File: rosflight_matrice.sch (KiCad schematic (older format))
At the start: 18 parts, among them J1 Left, J10 I2C, J11 I2C, J2 Right, J3 Power, J4 Servo 1-3, J5 Servo 4-6, J6 Main, J7 Flexi-IO, J8 Flexi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

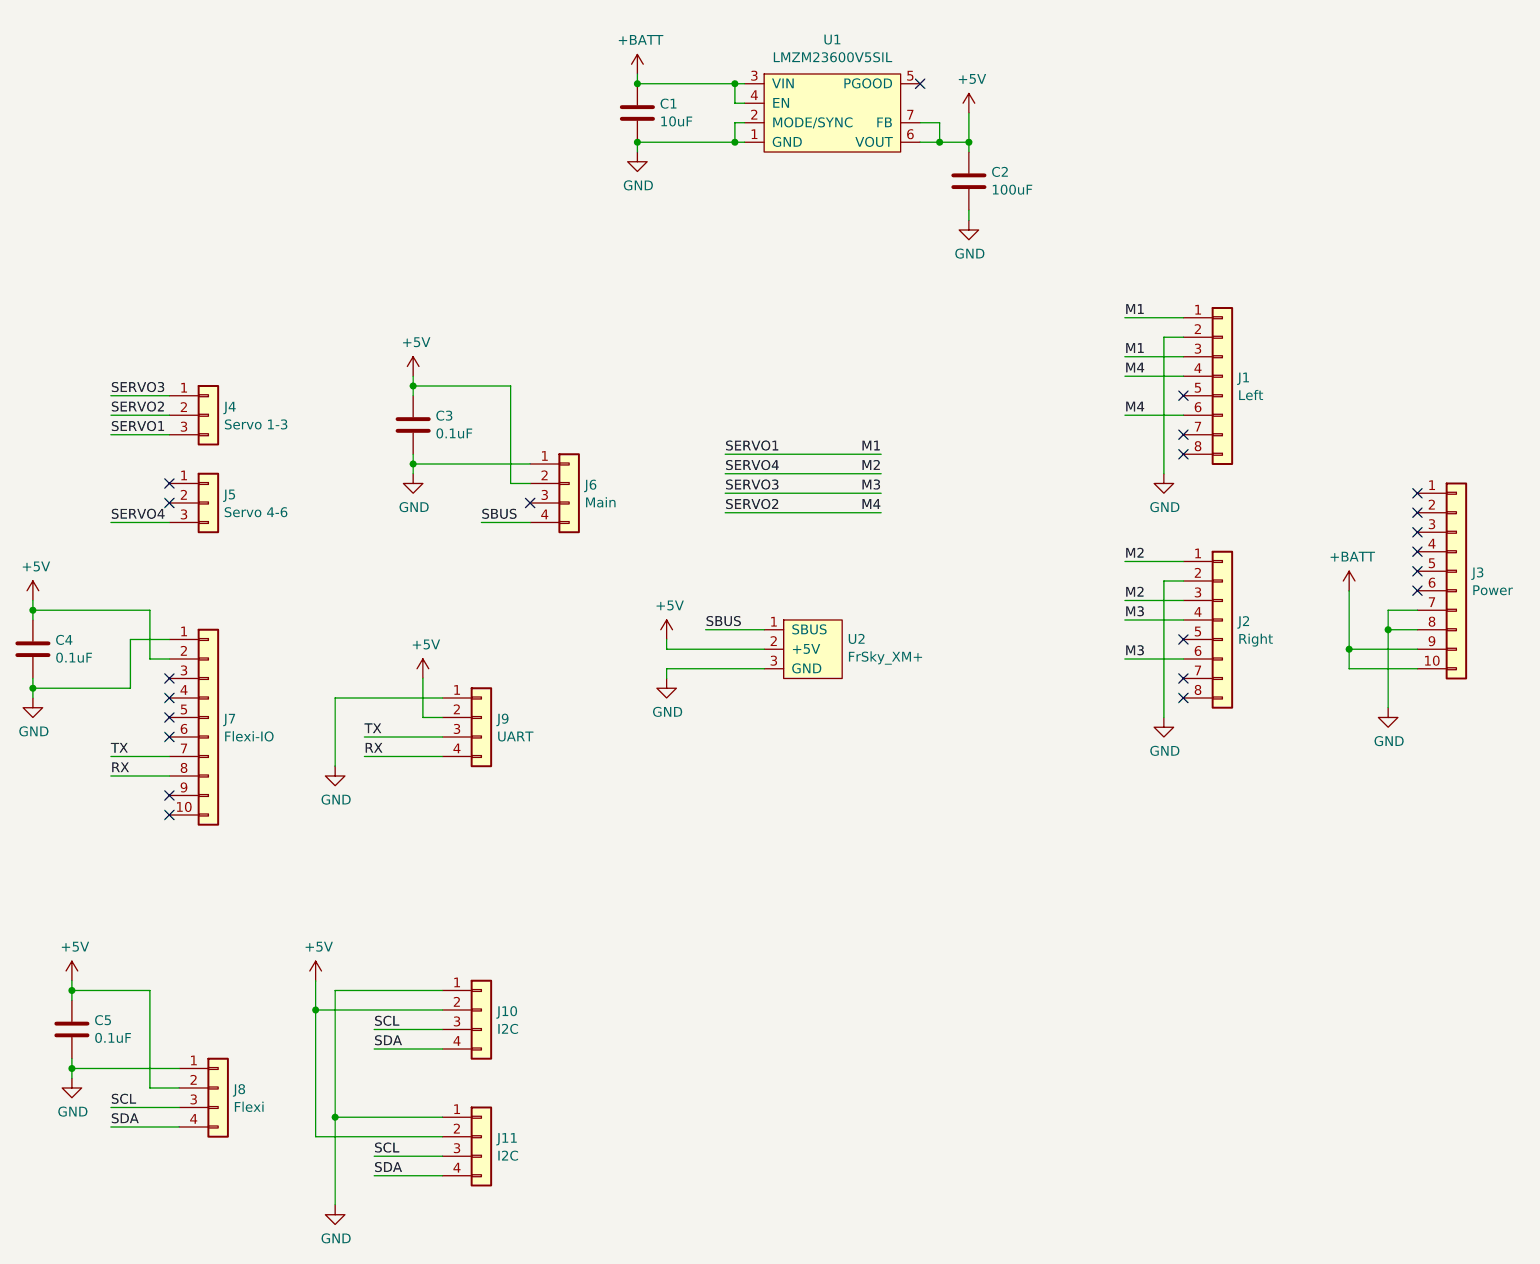
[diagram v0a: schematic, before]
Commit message: New switching voltage regulator and updated layout
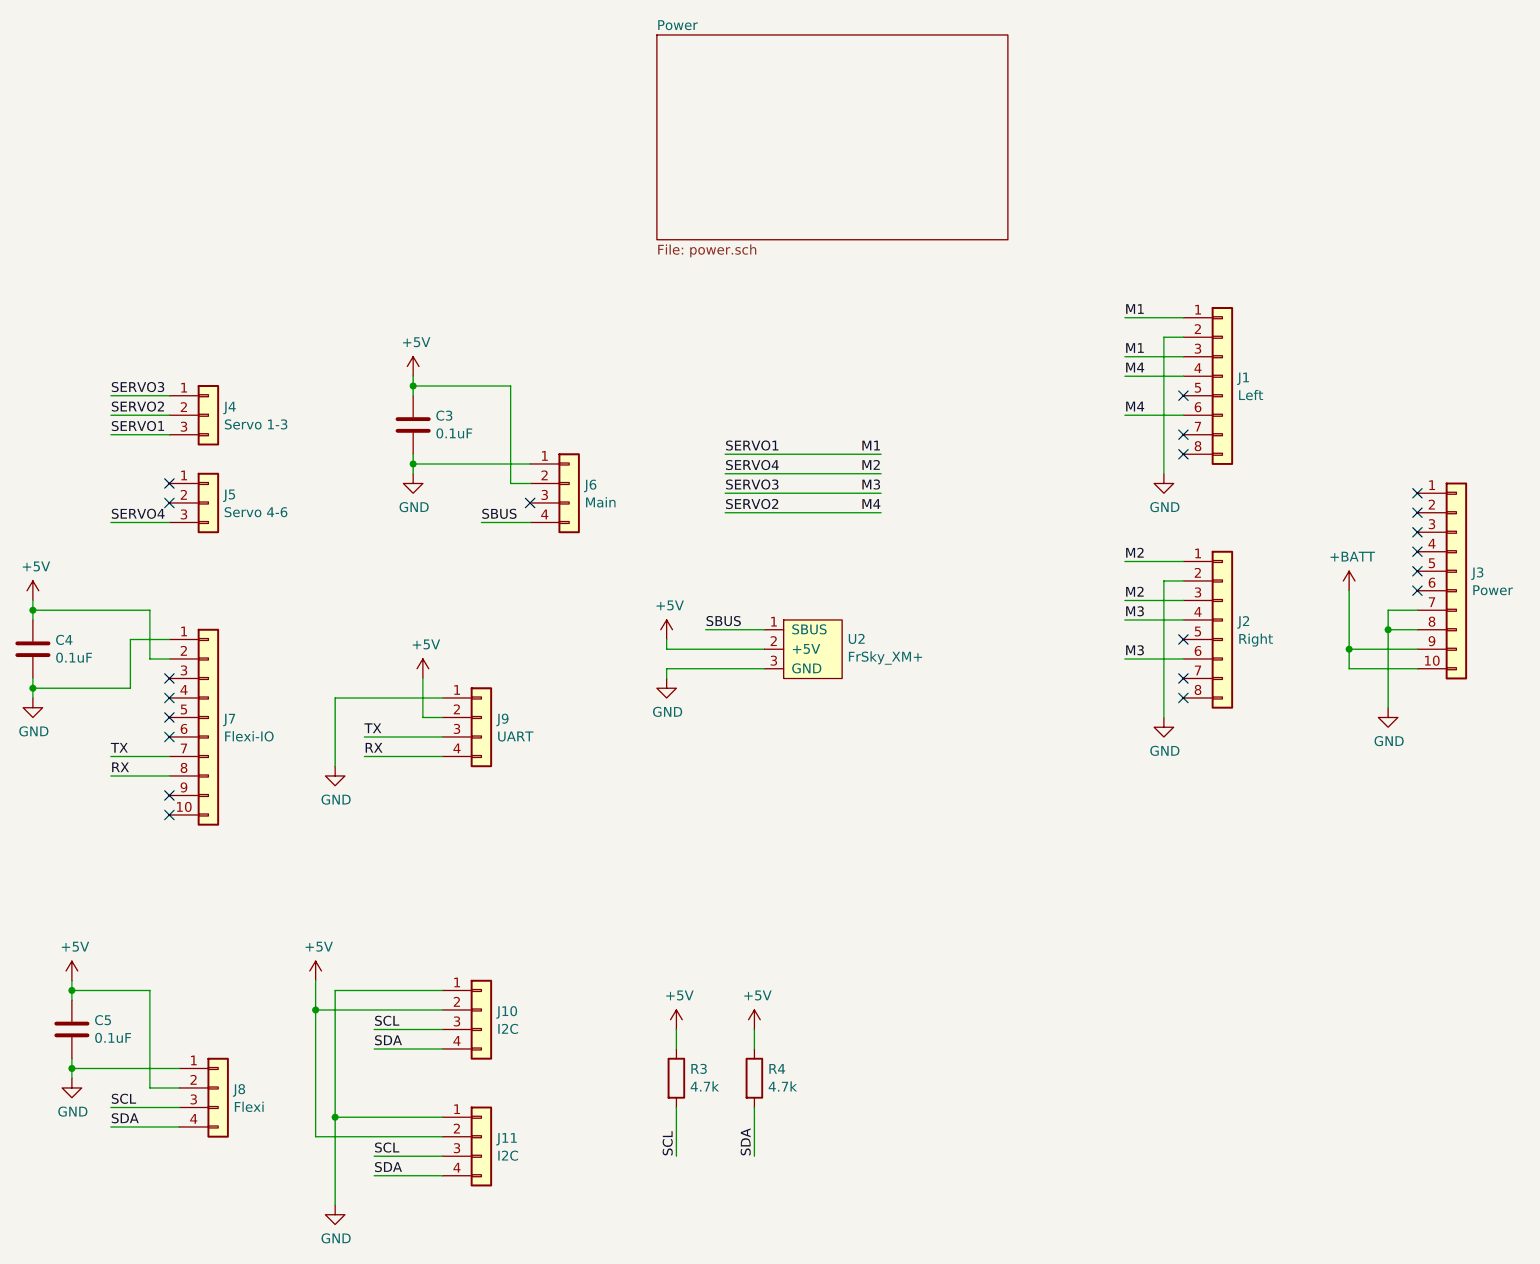
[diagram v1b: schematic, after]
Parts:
- removed C1: 10uF, Capacitor_SMD:C_1210_3225Metric_Pad1.42x2.65mm_HandSolder, symbol Device:C
- removed C2: 100uF, Capacitor_SMD:C_1206_3216Metric_Pad1.42x1.75mm_HandSolder, symbol Device:C
- removed U1: LMZM23600V5SIL, Package_LGA:Texas_SIL0010A_MicroSiP-10-1EP_3.8x3mm_P0.6mm_EP0.7x2.9mm_ThermalVias, symbol quadrotor:LMZM23600V5SIL
- added R3, R4: 4.7k, Resistor_SMD:R_0603_1608Metric_Pad1.05x0.95mm_HandSolder, symbol Device:R
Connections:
- net +5V: now also R3.1, R4.1
- net SCL: now also R3.2
- net SDA: now also R4.2
- no-connect marks 22 -> 21
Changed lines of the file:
@@
 $Descr A4 11693 8268
 encoding utf-8
-Sheet 1 1
+Sheet 1 2
 Title ""
 Date ""
@@
 Text Label 5000 4150 0    50   ~ 0
 SBUS
-$Comp
-L power:+BATT #PWR07
-U 1 1 5CCA1FE5
-P 4650 1300
-F 0 "#PWR07" H 4650 1150 50  0001 C CNN
-F 1 "+BATT" H 4665 1473 50  0000 C CNN
-F 2 "" H 4650 1300 50  0001 C CNN
-F 3 "" H 4650 1300 50  0001 C CNN
-	1    4650 1300
-	1    0    0    -1
-$EndComp
-$Comp
-L power:+5V #PWR09
-U 1 1 5CCA2018
-P 6350 1500
-F 0 "#PWR09" H 6350 1350 50  0001 C CNN
-F 1 "+5V" H 6365 1673 50  0000 C CNN
-F 2 "" H 6350 1500 50  0001 C CNN
-F 3 "" H 6350 1500 50  0001 C CNN
-	1    6350 1500
-	1    0    0    -1
-$EndComp
-$Comp
-L power:GND #PWR08
-U 1 1 5CCA204B
-P 4650 1700
-F 0 "#PWR08" H 4650 1450 50  0001 C CNN
-F 1 "GND" H 4655 1527 50  0000 C CNN
-F 2 "" H 4650 1700 50  0001 C CNN
-F 3 "" H 4650 1700 50  0001 C CNN
-	1    4650 1700
-	1    0    0    -1
-$EndComp
-$Comp
-L power:GND #PWR010
-U 1 1 5CCA2196
-P 6350 2050
-F 0 "#PWR010" H 6350 1800 50  0001 C CNN
-F 1 "GND" H 6355 1877 50  0000 C CNN
-F 2 "" H 6350 2050 50  0001 C CNN
-F 3 "" H 6350 2050 50  0001 C CNN
-	1    6350 2050
-	1    0    0    -1
-$EndComp
-$Comp
-L Device:C C1
-U 1 1 5CCA22B1
-P 4650 1500
-F 0 "C1" H 4765 1546 50  0000 L CNN
-F 1 "10uF" H 4765 1455 50  0000 L CNN
-F 2 "Capacitor_SMD:C_1210_3225Metric_Pad1.42x2.65mm_HandSolder" H 4688 1350 50  0001 C CNN
-F 3 "~" H 4650 1500 50  0001 C CNN
-	1    4650 1500
-	1    0    0    -1
-$EndComp
-$Comp
-L Device:C C2
-U 1 1 5CCA235A
-P 6350 1850
-F 0 "C2" H 6465 1896 50  0000 L CNN
-F 1 "100uF" H 6465 1805 50  0000 L CNN
-F 2 "Capacitor_SMD:C_1206_3216Metric_Pad1.42x1.75mm_HandSolder" H 6388 1700 50  0001 C CNN
-F 3 "~" H 6350 1850 50  0001 C CNN
-	1    6350 1850
-	1    0    0    -1
-$EndComp
-Wire Wire Line
-	6350 2000 6350 2050
-Wire Wire Line
-	6100 1650 6200 1650
-Wire Wire Line
-	6350 1650 6350 1500
-Wire Wire Line
-	6350 1650 6350 1700
-Connection ~ 6350 1650
-Wire Wire Line
-	6100 1550 6200 1550
-Wire Wire Line
-	6200 1550 6200 1650
-Connection ~ 6200 1650
-Wire Wire Line
-	6200 1650 6350 1650
-NoConn ~ 6100 1350
-Wire Wire Line
-	5200 1650 5150 1650
-Wire Wire Line
-	4650 1700 4650 1650
-Connection ~ 4650 1650
-Wire Wire Line
-	5200 1550 5150 1550
-Wire Wire Line
-	5150 1550 5150 1650
-Wire Wire Line
-	5200 1350 5150 1350
-Wire Wire Line
-	4650 1300 4650 1350
-Connection ~ 4650 1350
-Wire Wire Line
-	5200 1450 5150 1450
-Wire Wire Line
-	5150 1450 5150 1350
-Wire Wire Line
-	4650 1350 5150 1350
-Connection ~ 5150 1350
-Wire Wire Line
-	4650 1650 5150 1650
-Connection ~ 5150 1650
-$Comp
-L quadrotor:LMZM23600V5SIL U1
-U 1 1 5CCDBFB7
-P 5650 1500
-F 0 "U1" H 5650 1875 50  0000 C CNN
-F 1 "LMZM23600V5SIL" H 5650 1784 50  0000 C CNN
-F 2 "Package_LGA:Texas_SIL0010A_MicroSiP-10-1EP_3.8x3mm_P0.6mm_EP0.7x2.9mm_ThermalVias" H 5650 1150 50  0001 C CNN
-F 3 "http://www.ti.com/lit/ds/symlink/lmzm23600.pdf" H 5650 1050 50  0001 C CNN
-	1    5650 1500
-	1    0    0    -1
-$EndComp
+$Sheet
+S 4750 1100 1800 1050
+U 5CE724BA
+F0 "Power" 50
+F1 "power.sch" 50
+$EndSheet
+$Comp
+L Device:R R3
+U 1 1 5D203B8D
+P 4850 6450
+F 0 "R3" H 4920 6496 50  0000 L CNN
+F 1 "4.7k" H 4920 6405 50  0000 L CNN
+F 2 "Resistor_SMD:R_0603_1608Metric_Pad1.05x0.95mm_HandSolder" V 4780 6450 50  0001 C CNN
+F 3 "~" H 4850 6450 50  0001 C CNN
+	1    4850 6450
+	1    0    0    -1
+$EndComp
+$Comp
+L Device:R R4
+U 1 1 5D203CEA
+P 5250 6450
+F 0 "R4" H 5320 6496 50  0000 L CNN
+F 1 "4.7k" H 5320 6405 50  0000 L CNN
+F 2 "Resistor_SMD:R_0603_1608Metric_Pad1.05x0.95mm_HandSolder" V 5180 6450 50  0001 C CNN
+F 3 "~" H 5250 6450 50  0001 C CNN
+	1    5250 6450
+	1    0    0    -1
+$EndComp
+$Comp
+L power:+5V #PWR010
+U 1 1 5D203E0E
+P 4850 6200
+F 0 "#PWR010" H 4850 6050 50  0001 C CNN
+F 1 "+5V" H 4865 6373 50  0000 C CNN
+F 2 "" H 4850 6200 50  0001 C CNN
+F 3 "" H 4850 6200 50  0001 C CNN
+	1    4850 6200
+	1    0    0    -1
+$EndComp
+$Comp
+L power:+5V #PWR011
+U 1 1 5D203E3B
+P 5250 6200
+F 0 "#PWR011" H 5250 6050 50  0001 C CNN
+F 1 "+5V" H 5265 6373 50  0000 C CNN
+F 2 "" H 5250 6200 50  0001 C CNN
+F 3 "" H 5250 6200 50  0001 C CNN
+	1    5250 6200
+	1    0    0    -1
+$EndComp
+Wire Wire Line
+	4850 6300 4850 6200
+Wire Wire Line
+	5250 6300 5250 6200
+Wire Wire Line
+	4850 6600 4850 6850
+Wire Wire Line
+	5250 6600 5250 6850
+Text Label 4850 6850 1    50   ~ 0
+SCL
+Text Label 5250 6850 1    50   ~ 0
+SDA
 $EndSCHEMATC
